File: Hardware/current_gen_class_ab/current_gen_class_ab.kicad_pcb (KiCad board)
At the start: 4 copper layers, 100 x 100 mm, 79 parts, among them J1 Conn_Coaxial, J2 Conn_Coaxial, J3 Conn_01x01_Socket, J4 Conn_01x01_Socket, J5 Conn_01x01_Socket, J6 Conn_01x01_Socket, J7 Conn_01x01_Socket, Q1 PMOS, Q2 NMOS, Q3 NMOS, Q4 PMOS, U1 Opamp_Dual, U2 Opamp_Dual

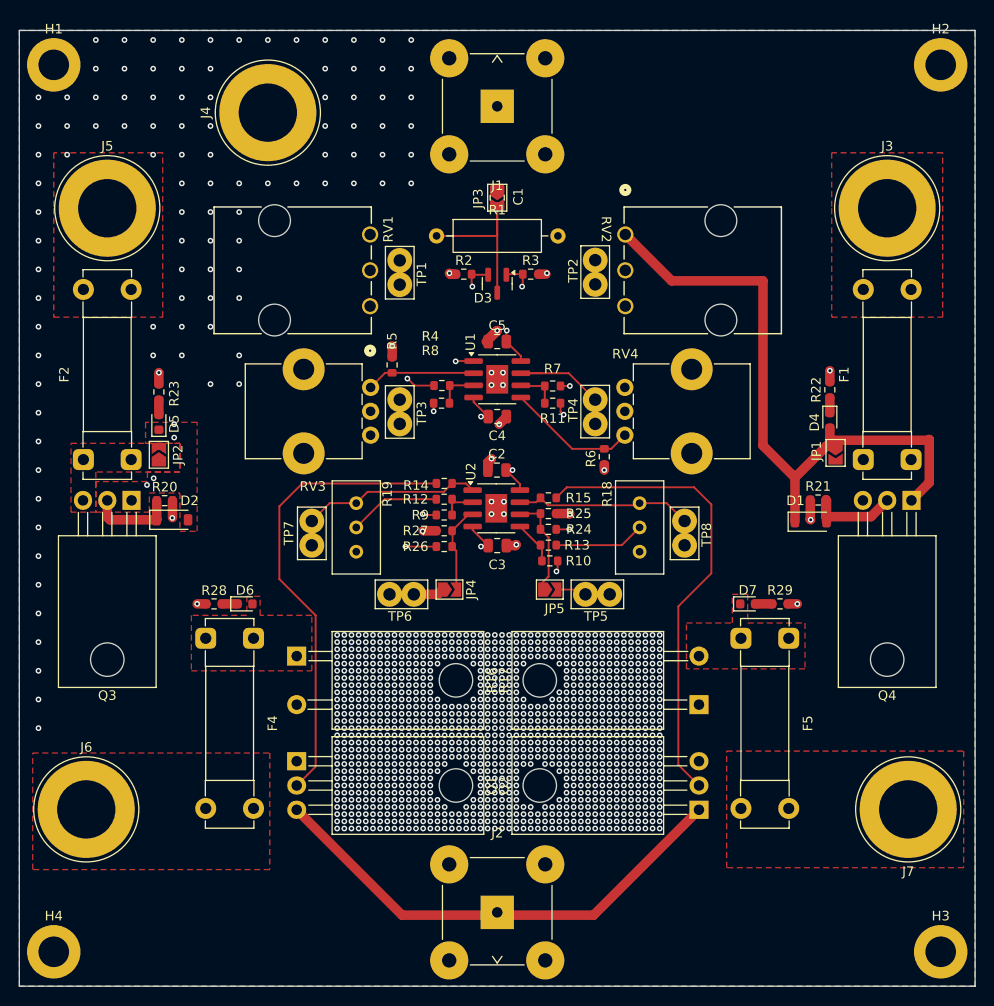
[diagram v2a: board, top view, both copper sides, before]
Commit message: stitch and slikscreened
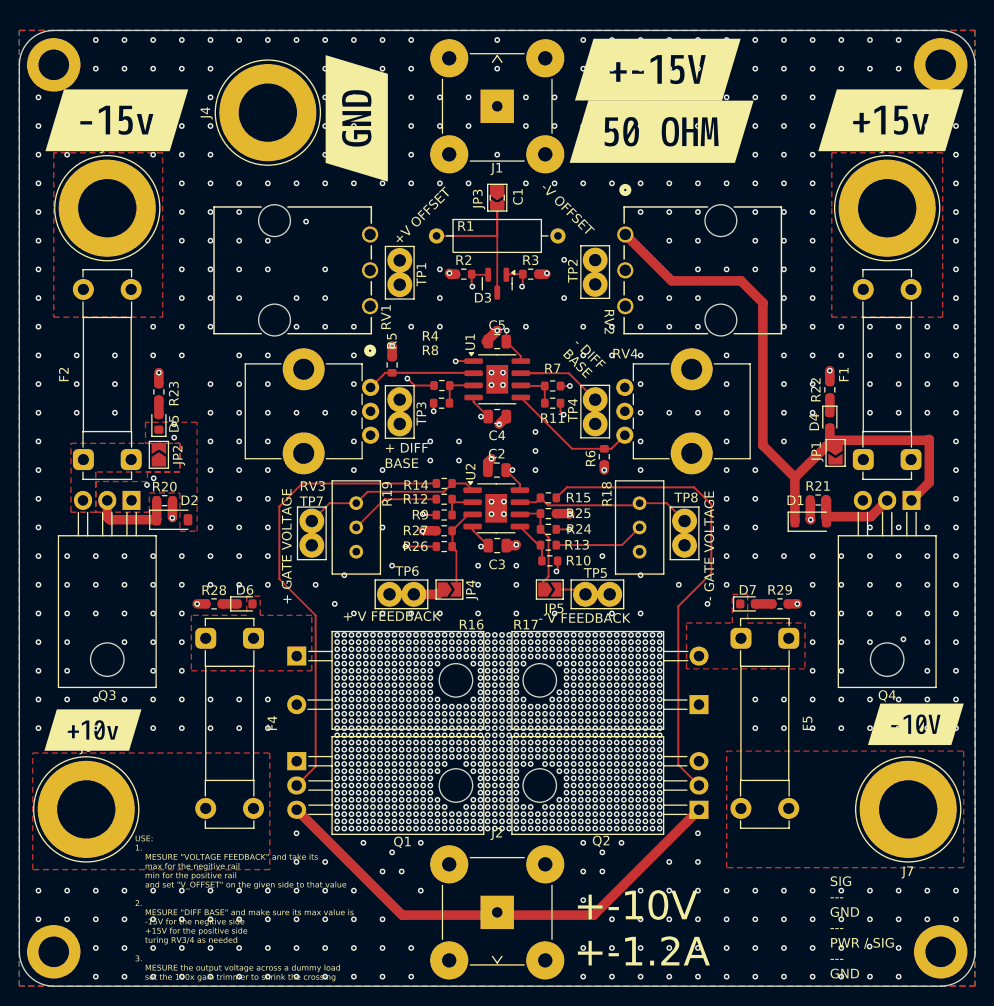
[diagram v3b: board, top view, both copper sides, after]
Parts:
- added kibuzzard-68929C33: G***, kibuzzard-68929C33, F.Cu at (119.2, 69.4)
- added kibuzzard-68929C42: G***, kibuzzard-68929C42, F.Cu at (200.2, 69.4)
- added kibuzzard-68929C79: G***, kibuzzard-68929C79, F.Cu at (175.8, 64.1)
- added kibuzzard-68929C81: G***, kibuzzard-68929C81, F.Cu at (176.2, 70.6)
- added kibuzzard-68929C8D: G***, kibuzzard-68929C8D, F.Cu at (144.3, 69.2)
- added kibuzzard-68929CA4: G***, kibuzzard-68929CA4, F.Cu at (116.7, 133.2)
- added kibuzzard-68929CB0: G***, kibuzzard-68929CB0, F.Cu at (202.8, 132.6)
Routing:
- net +15V: track 113.1 -> 111.8 mm
- net GND: vias 1291 -> 1744
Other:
- outline, holes or cut-outs redrawn
- board text added: "+ DIFF BASE"
- board text added: "+ GATE VOLTAGE"
- board text added: "+ V FEEDBACK"
- board text added: "+-10V +-1.2A"
- board text added: "+V OFFSET"
- board text added: "- DIFF BASE"
- board text added: "- GATE VOLTAGE"
- board text added: "- V FEEDBACK"
- board text added: "-V OFFSET"
- board text added: "SIG --- GND --- PWR / SIG --- GND"
- board text added: "USE: 1. MESURE {dblquote}VOLTAGE FEEDBACK{dblquote} and take its max for the negitive rail min for the positive rail and set {dblquote}V_OFFSET{dblquote} on the given side to that value 2. MESURE {dblquote}DIFF BASE{dblquote} and make sure its max value is -15V for the negitive side +15V for the positive side turing RV3/4 as needed 3. MESURE the output voltage across a dummy load set the 100x gai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"

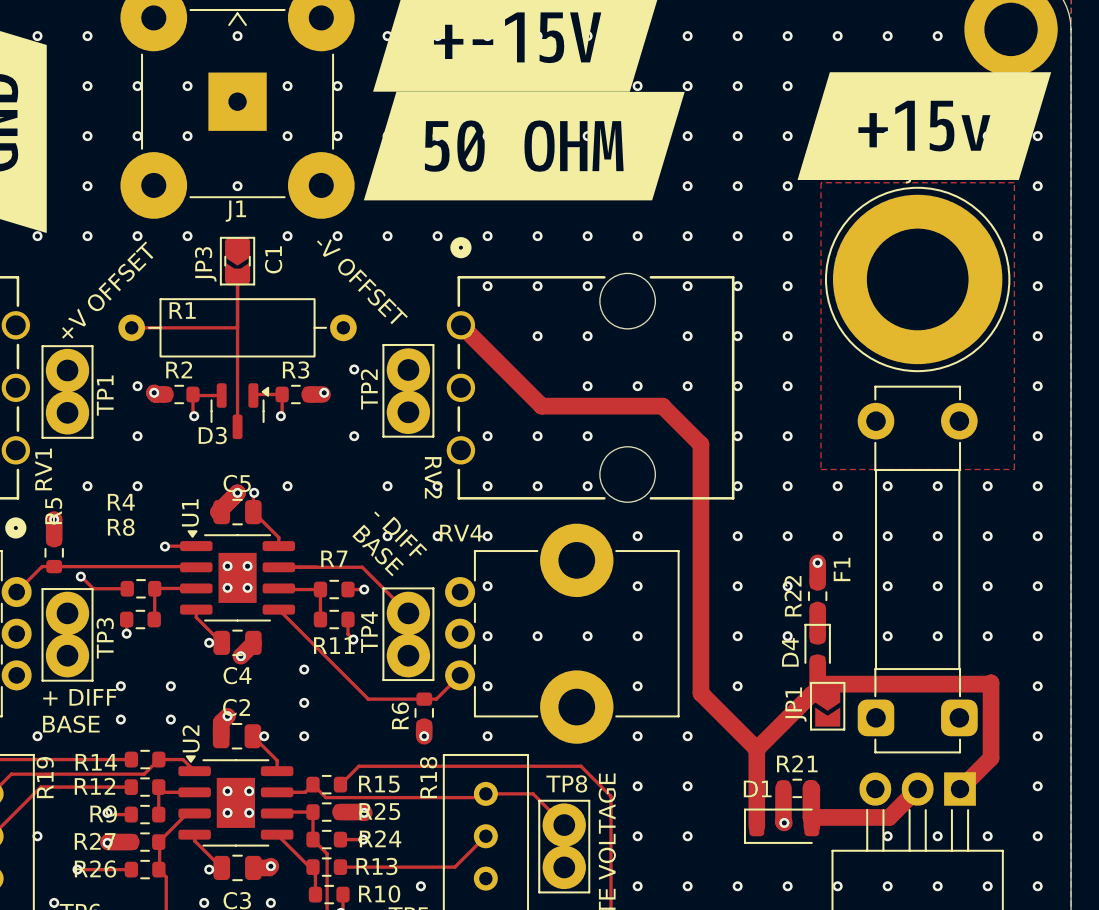
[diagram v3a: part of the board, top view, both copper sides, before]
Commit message: updated fill zones and fixed some routing
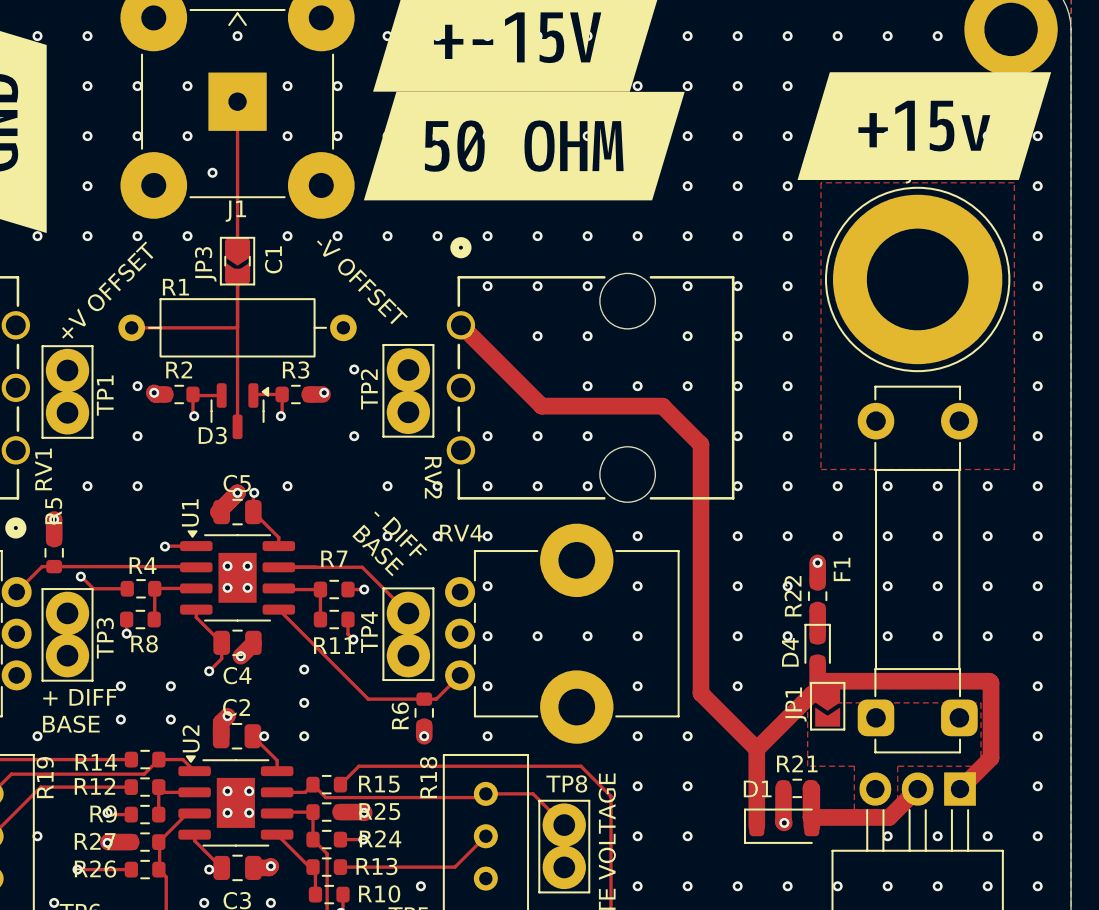
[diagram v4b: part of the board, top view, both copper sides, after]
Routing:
- net Net-(J1-In): track 0.00 -> 8.62 mm
- net -15V: track 102.9 -> 104.2 mm
- added copper zone on F.Cu, net Net-(JP1-B)
- removed copper zone on In2.Cu, net Net-(JP1-B)
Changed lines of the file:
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@@
 				(font
 					(size 0.001 0.001)
+					(thickness 0.15)
 				)
 			)
@@
 				(font
 					(size 0.001 0.001)
+					(thickness 0.15)
 				)
 			)
@@
 				(font
 					(size 0.001 0.001)
+					(thickness 0.15)
 				)
 			)
@@
 				(font
 					(size 0.001 0.001)
+					(thickness 0.15)
 				)
 			)
@@
 				(font
 					(size 0.001 0.001)
+					(thickness 0.15)
 				)
 			)
@@
 				(font
 					(size 0.001 0.001)
+					(thickness 0.15)
 				)
 			)
@@
 				(font
 					(size 0.001 0.001)
+					(thickness 0.15)
 				)
 			)
@@
 				(font
 					(size 0.001 0.001)
+					(thickness 0.15)
 				)
 			)
@@
 				(font
 					(size 0.001 0.001)
+					(thickness 0.15)
 				)
 			)
@@
 				(font
 					(size 0.001 0.001)
+					(thickness 0.15)
 				)
 			)
@@
 				(font
 					(size 0.001 0.001)
+					(thickness 0.15)
 				)
 			)
@@
 				(font
 					(size 0.001 0.001)
+					(thickness 0.15)
 				)
 			)
@@
 		(tags "resistor")
 		(property "Reference" "R4"
-			(at 1.21 5.155 0)
+			(at -0.09 1.355 0)
 			(layer "F.SilkS")
 			(effects
@@
 		(tags "Resistor Axial_DIN0309 series Axial Horizontal pin pitch 12.7mm 0.5W = 1/2W length 9mm diameter 3.2mm")
 		(property "Reference" "R1"
-			(at 3.05 -1 0)
+			(at 2.65 -2.4 0)
 			(layer "F.SilkS")
 			(effects
@@
 		(tags "resistor")
 		(property "Reference" "R8"
-			(at -1.175 -5.5 0)
+			(at 0.225 1.5 0)
 			(layer "F.SilkS")
 			(effects
@@
 				(font
 					(size 0.001 0.001)
+					(thickness 0.15)
 				)
 			)
@@
 				(font
 					(size 0.001 0.001)
+					(thickness 0.15)
 				)
 			)
@@
 	)
 	(segment
-		(start 158.05 100.4)
-		(end 157.299 100.4)
+		(start 158.050001 113.9)
+		(end 157.399 113.9)
 		(width 0.2)
 		(layer "F.Cu")
@@
 	(segment
 		(start 158.050001 113.9)
-		(end 157.399 113.9)
+		(end 156.425 112.274999)
 		(width 0.2)
 		(layer "F.Cu")
@@
 	)
 	(segment
-		(start 158.050001 113.9)
-		(end 156.425 112.274999)
+		(start 158.05 101.349)
+		(end 157.299 102.1)
+		(width 0.2)
+		(layer "F.Cu")
+		(net 1)
+	)
+	(segment
+		(start 158.05 100.4)
+		(end 158.05 101.349)
 		(width 0.2)
 		(layer "F.Cu")
@@
 	)
 	(via
-		(at 157.299 100.4)
+		(at 157.299 102.1)
 		(size 0.6)
 		(drill 0.3)
@@
 	)
 	(segment
-		(start 125.2 102.6)
-		(end 125.2 104.71)
+		(start 157.299 102.1)
+		(end 157.299 114)
 		(width 1)
 		(layer "In2.Cu")
@@
 	)
 	(segment
-		(start 143.6 79.4519)
-		(end 143.133199 79.4519)
+		(start 125.2 102.6)
+		(end 125.2 104.71)
 		(width 1)
 		(layer "In2.Cu")
@@
 	)
 	(segment
-		(start 157.299 87.701)
-		(end 157.299 100.4)
+		(start 143.6 79.4519)
+		(end 143.133199 79.4519)
 		(width 1)
 		(layer "In2.Cu")
@@
 	)
 	(segment
-		(start 122.355 107.555)
-		(end 120.74 109.17)
+		(start 152.836272 79.4519)
+		(end 143.6 79.4519)
 		(width 1)
 		(layer "In2.Cu")
@@
 	)
 	(segment
-		(start 157.299 100.4)
-		(end 157.299 114)
+		(start 122.355 107.555)
+		(end 120.74 109.17)
 		(width 1)
 		(layer "In2.Cu")
@@
 	)
 	(segment
-		(start 157.785372 87.214628)
-		(end 157.299 87.701)
+		(start 157.299 87.701)
+		(end 157.8 87.2)
 		(width 1)
 		(layer "In2.Cu")
@@
 	)
 	(segment
-		(start 157.8 87.2)
-		(end 157.785372 87.214628)
-		(width 1)
-		(layer "In2.Cu")
-		(net 1)
-	)
-	(segment
-		(start 143.6 79.4519)
+		(start 157.8 84.415628)
 		(end 152.836272 79.4519)
 		(width 1)
@@
 	)
 	(segment
-		(start 157.8 84.415628)
-		(end 157.8 87.2)
+		(start 157.8 87.2)
+		(end 157.8 84.415628)
 		(width 1)
 		(layer "In2.Cu")
@@
 	)
 	(segment
-		(start 152.836272 79.4519)
-		(end 157.8 84.415628)
+		(start 157.299 102.1)
+		(end 157.299 87.701)
 		(width 1)
 		(layer "In2.Cu")
@@
 	)
 	(segment
-		(start 159.95 100.4)
-		(end 159.95 100.45)
-		(width 1)
-		(layer "F.Cu")
-		(net 2)
-	)
-	(segment
 		(start 165.175 110.55)
 		(end 166.55 110.55)
@@
 	)
 	(segment
-		(start 159.95 100.45)
-		(end 159.2 101.2)
-		(width 1)
-		(layer "F.Cu")
-		(net 2)
-	)
-	(segment
 		(start 154 85.4)
 		(end 154.1 85.5)
@@
 	)
 	(segment
+		(start 159.2 101.2)
+		(end 159.95 100.45)
+		(width 1)
+		(layer "F.Cu")
+		(net 2)
+	)
+	(segment
+		(start 159.95 100.45)
+		(end 159.95 100.4)
+		(width 1)
+		(layer "F.Cu")
+		(net 2)
+	)
+	(segment
 		(start 191.75 111.15)
 		(end 191.8 111.2)
@@
 	)
 	(via
-		(at 159 73)
+		(at 157.5 72.2)
 		(size 0.6)
 		(drill 0.3)
@@
 	)
 	(segment
-		(start 204.2 107.31)
-		(end 202.34 109.17)
+		(start 193.975001 102.7)
+		(end 204.1 102.7)
+		(width 1)
+		(layer "F.Cu")
+		(net 5)
+	)
+	(segment
+		(start 204.2 102.8)
+		(end 204.2 107.31)
 		(width 1)
 		(layer "F.Cu")
@@
 	)
 	(segment
-		(start 204.2 102.8)
-		(end 204.2 107.31)
+		(start 204.2 107.31)
+		(end 202.34 109.17)
 		(width 1)
 		(layer "F.Cu")
@@
 	)
 	(segment
+		(start 193.8 102.875001)
+		(end 193.975001 102.7)
+		(width 1)
+		(layer "F.Cu")
+		(net 5)
+	)
+	(segment
 		(start 159.95 92.555)
 		(end 161.475 94.08)
@@
 	)
 	(segment
-		(start 159.92 106)
-		(end 161.375 107.455)
-		(width 0.2)
+		(start 204.1 102.7)
+		(end 204.2 102.8)
+		(width 1)
 		(layer "F.Cu")
 		(net 5)
 	)
 	(segment
-		(start 204.124999 102.875001)
-		(end 204.2 102.8)
-		(width 1)
+		(start 159.92 106)
+		(end 161.375 107.455)
+		(width 0.2)
 		(layer "F.Cu")
 		(net 5)
@@
 	)
 	(segment
-		(start 193.8 102.875001)
-		(end 204.124999 102.875001)
-		(width 1)
-		(layer "F.Cu")
-		(net 5)
-	)
-	(segment
 		(start 193.451562 103.475001)
 		(end 194.4 103.475001)
@@
 	)
 	(segment
+		(start 159 67.935)
+		(end 159 76.550001)
+		(width 0.2)
+		(layer "F.Cu")
+		(net 17)
+	)
+	(segment
 		(start 169.085 152.565)
 		(end 180.11 141.54)
@@
 	)
 	(segment
+		(start 197.260001 104.939999)
+		(end 197.3 104.9)
+		(width 0.2)
+		(layer "In2.Cu")
+		(net 21)
+	)
+	(segment
 		(start 136.2 109.8)
 		(end 138.6 107.4)
@@
 		(hatch edge 0.5)
 		(priority 9)
-		(connect_pads
+		(connect_pads yes
 			(clearance 0.5)
 		)
@@
 		(hatch edge 0.5)
 		(priority 10)
-		(connect_pads
+		(connect_pads yes
 			(clearance 0.5)
 		)
@@
 		(hatch edge 0.5)
 		(priority 10)
-		(connect_pads
+		(connect_pads yes
 			(clearance 0.5)
 		)
@@
 	)
 	(zone
+		(net 21)
+		(net_name "Net-(JP1-B)")
+		(layer "F.Cu")
+		(hatch edge 0.5)
+		(priority 10)
+		(connect_pads yes
+			(clearance 0.5)
+		)
+		(min_thickness 0.25)
+		(filled_areas_thickness no)
+		(fill yes
+			(thermal_gap 0.5)
+			(thermal_bridge_width 0.5)
+		)
+		(polygon
+			(pts
+				(xy 193.2 104) (xy 203.6 104) (xy 203.6 107.8) (xy 198.6 107.8) (xy 198.6 110.4) (xy 196 110.4)
+				(xy 196 107.8) (xy 193.2 107.8)
+			)
+		)
+	)
+	(zone
 		(net 2)
 		(net_name "GND")
@@
 		(hatch edge 0.5)
 		(priority 6)
-		(connect_pads
+		(connect_pads yes
 			(clearance 0.5)
 		)
@@
 		(hatch edge 0.5)
 		(priority 1)
-		(connect_pads
+		(connect_pads yes
 			(clearance 0.5)
 		)
@@
 			)
 		)
-	)
-	(zone
-		(net 21)
-		(net_name "Net-(JP1-B)")
-		(layer "In2.Cu")
-		(hatch edge 0.5)
-		(priority 5)
-		(connect_pads
-			(clearance 0.5)
-		)
-		(min_thickness 0.25)
-		(filled_areas_thickness no)
-		(fill yes
-			(thermal_gap 0.5)
-			(thermal_bridge_width 0.5)
-		)
-		(polygon
-			(pts
-				(xy 193.2 104) (xy 203.6 104) (xy 203.6 107.8) (xy 198.6 107.8) (xy 198.6 110.4) (xy 196 110.4)
-				(xy 196 107.8) (xy 193.2 107.8)
-			)
-		)
